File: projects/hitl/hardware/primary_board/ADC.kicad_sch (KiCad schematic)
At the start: 33 parts, among them J11 CONN_01X03, J12 CONN_01X03, J16 CONN_01X03, J17 CONN_01X03, J18 CONN_01X03, J19 CONN_01X03, U6 AD7091R-5BRUZ, U7 MCP6001, U8 74HCT4051D

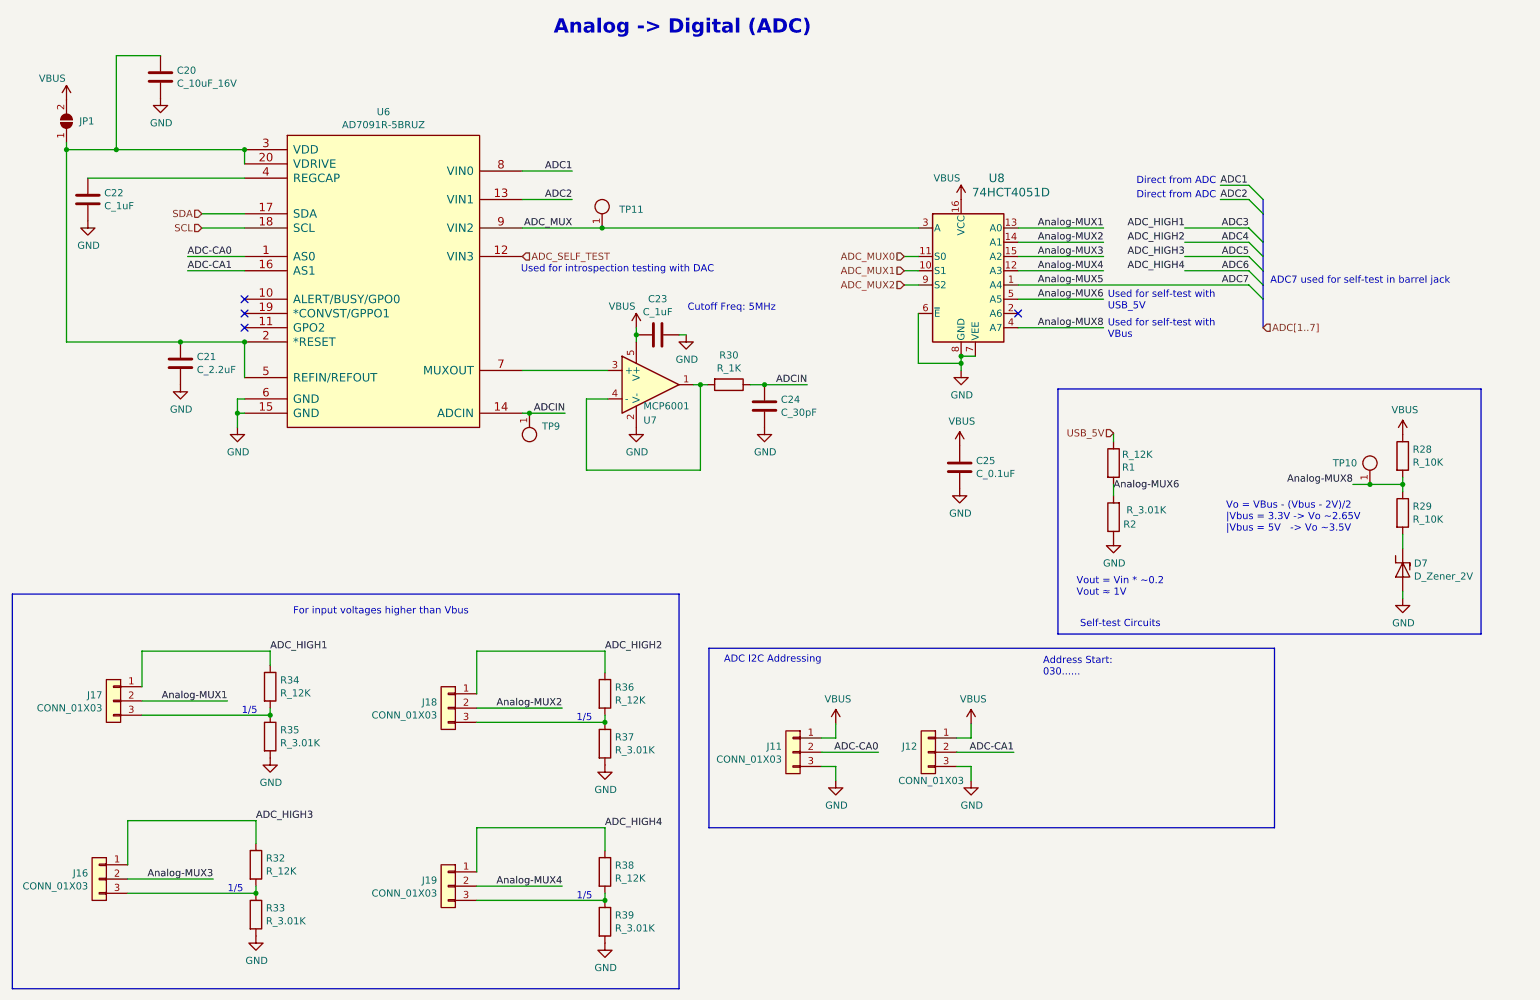
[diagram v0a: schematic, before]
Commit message: spec parts for hitl
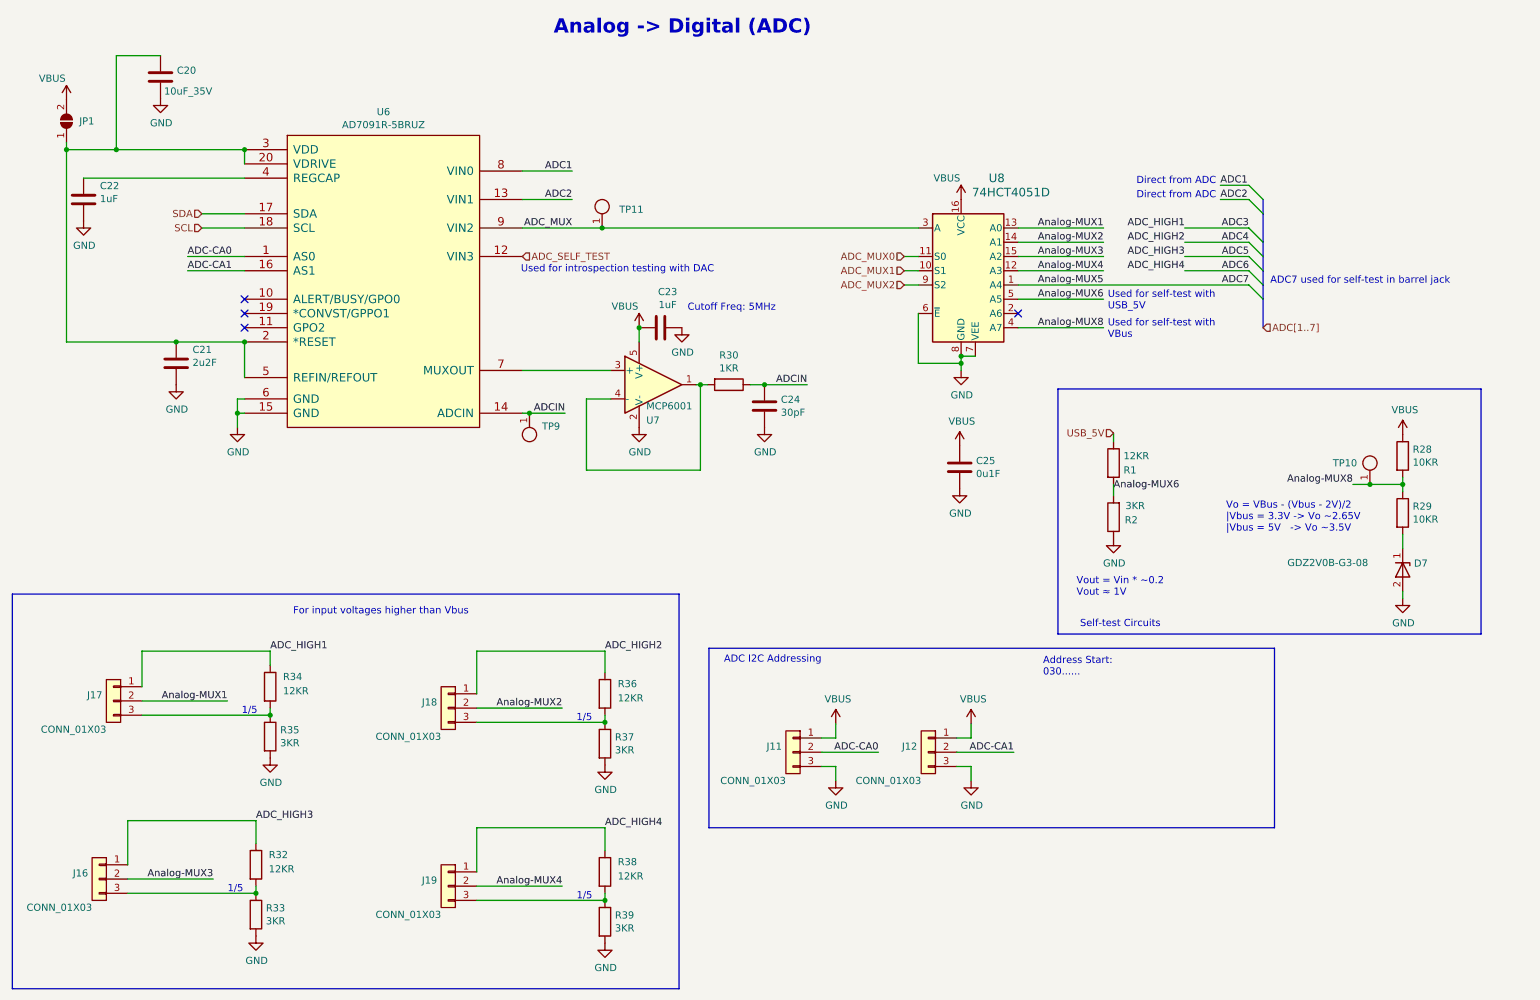
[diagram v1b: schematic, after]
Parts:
- C20: value C_10uF_16V -> 10uF_35V; footprint footprints:C_0805_OEM -> OEM:C_0603; symbol formula:C_10uF_16V -> OEM:10uF_35V; DKPN (none) -> 490-GRM188R6YA106MA73JDKR-ND; MFN DK -> Murata; MPN 1276-2399-1-ND -> GRM188R6YA106MA73J; NewDesigns (none) -> YES; Package (none) -> 0603; PurchasingLink https://www.digikey.com/product-detail/en/samsung-electro-m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 -> (none); Stocked (none) -> Digi-Reel; Style (none) -> SMD
- C21: value C_2.2uF -> 2u2F; footprint footprints:C_0805_OEM -> OEM:C_0603; symbol formula:C_2.2uF -> OEM:2u2F; DKPN (none) -> 490-GRM188R61E225KA12JDKR-ND; MFN (none) -> Murata; MPN (none) -> GRM188R61E225KA12J; NewDesigns (none) -> YES; Package (none) -> 0603; PurchasingLink https://www.digikey.com/product-detail/en/tdk-corporation/C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 -> (none); Stocked (none) -> Digi-Reel; Style (none) -> SMD
- C22, C23: value C_1uF -> 1uF; footprint footprints:C_0805_OEM -> OEM:C_0603; symbol formula:C_1uF -> OEM:1uF; DKPN (none) -> 1276-1184-2-ND; MFN (none) -> Samsung Electro-Mechanics; MPN (none) -> CL10B105KA8NNNC; NewDesigns (none) -> YES; Package (none) -> 0603; PurchasingLink https://www.digikey.com/product-detail/en/yageo/CC0805ZKY5V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 -> (none); Stocked (none) -> Reel; Style (none) -> SMD
- C24: value C_30pF -> 30pF; footprint footprints:C_0805_OEM -> OEM:C_0603; symbol formula:C_30pF -> OEM:30pF; DKPN (none) -> 738-CML0603C0G300JT50VDKR-ND; MFN DK -> Stackpole Electronics; MPN 1276-1130-1-ND -> CML0603C0G300JT50V; NewDesigns (none) -> YES; Package (none) -> 0603; PurchasingLink https://www.digikey.com/product-detail/en/samsung-electro-m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 -> (none); Stocked (none) -> Digi-Reel; Style (none) -> SMD
- C25: value C_0.1uF -> 0u1F; footprint footprints:C_0805_OEM -> OEM:C_0603; symbol formula:C_0.1uF -> OEM:0u1F; DKPN (none) -> 1276-1935-2-ND; MFN DK -> Samsung Electro-Mechanics; MPN 478-3352-1-ND -> CL10B104KB8NNWC; NewDesigns (none) -> YES; Package (none) -> 0603; PurchasingLink https://www.digikey.com/products/en?keywords=478-3352-1-ND -> (none); Stocked (none) -> Reel; Style (none) -> SMD
- D7: value D_Zener_2V -> GDZ2V0B-G3-08; symbol formula:D_Zener_2V -> OEM:GDZ2V0B-G3-08; DKPN (none) -> GDZ2V0B-G3-08GIDKR-ND; NewDesigns (none) -> YES; Package (none) -> SOD-323; PurchasingLink https://www.digikey.com/en/products/detail/vishay-general-s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 -> (none); Stocked (none) -> Digi-Reel; Style (none) -> SMD
- J11, J12, J16, J17, J18, J19: symbol formula:CONN_01X03 -> OEM:CONN_01X03; DKPN (none) -> 2057-PH1-03-UA-ND; MFN Mouser -> Adam Tech; MPN 855-M20-9990346 -> PH1-03-UA; NewDesigns (none) -> YES; Package (none) -> .1" pin header; PurchasingLink https://www.mouser.com/ProductDetail/Harwin/M20-9990346?qs=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 -> (none); Stocked (none) -> Bulk; Style (none) -> THT
- JP1: now left out of the parts list
- R1, R32, R34, R36, R38: value R_12K -> 12KR; footprint footprints:R_0805_OEM -> OEM:R_0603; symbol formula:R_12K -> OEM:12KR; DKPN (none) -> 1292-WR06X153JTLTR-ND; MFN TE -> Stackpole Electronics; MPN CRGP0805F12K -> RMCF0603FT12K0; NewDesigns (none) -> YES; Package (none) -> 0603; PurchasingLink https://www.digikey.com/en/products/detail/te-connectivity-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 -> (none); Stocked (none) -> Reel; Style (none) -> SMD
- R2, R33, R35, R37, R39: value R_3.01K -> 3KR; footprint footprints:R_0805_OEM -> OEM:R_0603; symbol formula:R_3.01K -> OEM:3KR; DKPN (none) -> 13-RC0603FR-103KLDKR-ND; MFN DK -> Yageo; MPN 311-3.01KCRCT-ND -> RC0603FR-103KL; NewDesigns (none) -> YES; Package (none) -> 0603; PurchasingLink https://www.digikey.com/products/en?keywords=311-3.01KCRCT-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 -> (none); Stocked (none) -> Digi-Reel; Style (none) -> SMD
- R28, R29: value R_10K -> 10KR; footprint footprints:R_0805_OEM -> OEM:R_0603; symbol formula:R_10K -> OEM:10KR; DKPN (none) -> RMCF0603FT10K0TR-ND; MFN DK -> Stackpole Electronics; MPN CRS0805-FX-1002ELFCT-ND -> RMCF0603FT10K0; NewDesigns (none) -> YES; Package (none) -> 0603; PurchasingLink https://www.digikey.com/products/en?keywords=CRS0805-FX-100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 -> (none); Stocked (none) -> Reel; Style (none) -> SMD
- R30: value R_1K -> 1KR; footprint footprints:R_0805_OEM -> OEM:R_0603; symbol formula:R_1K -> OEM:1KR; DKPN (none) -> RMCF0603FT1K00TR-ND; MFN DK -> Stackpole Electronics; MPN RNCP0805FTD1K00CT-ND -> RMCF0603FT1K00; NewDesigns (none) -> YES; Package (none) -> 0603; PurchasingLink https://www.digikey.com/products/en?keywords=RNCP0805FTD1K0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 -> (none); Stocked (none) -> Reel; Style (none) -> SMD
- TP10, TP11, TP9: value Test_Point_SMD -> TP_SMD; symbol formula:Test_Point_SMD -> OEM:TP_SMD; DKPN (none) -> 36-5019TR-ND; MFN (none) -> Keystone; MPN (none) -> 5019; NewDesigns (none) -> YES; Package (none) -> Custom; Stocked (none) -> Reel; Style (none) -> SMD
- U7: footprint footprints:SOT-23-5_OEM -> OEM:SOT-23-5; symbol formula:MCP6001 -> OEM:MCP6001; DKPN (none) -> MCP6001T-I/OTCT-ND; MFN DK -> Microchip; MPN MCP6001T-I/OTCT-ND -> MCP6001T-I/OT; NewDesigns (none) -> YES; Package (none) -> SOT23-5; PurchasingLink https://www.digikey.com/product-detail/en/microchip-technol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 -> (none); Stocked (none) -> Tape; Style (none) -> SMD
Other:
- moved on the sheet: C21, C22, C23, U7

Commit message: generate gerbs, fix leds and mcp6001s
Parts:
- U7: footprint OEM:SOT-23-5 -> Package_TO_SOT_SMD:SOT-353_SC-70-5; Package SOT23-5 -> SC-70-5
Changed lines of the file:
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@@
       (effects (font (size 1.27 1.27)) (justify left))
     )
-    (property "Footprint" "OEM:SOT-23-5" (id 2) (at 132.08 83.82 0)
+    (property "Footprint" "Package_TO_SOT_SMD:SOT-353_SC-70-5" (id 2) (at 132.08 83.82 0)
       (effects (font (size 1.27 1.27)) hide)
     )
@@
       (effects (font (size 1.27 1.27)) hide)
     )
-    (property "Package" "SOT23-5" (id 7) (at 134.62 86.36 0)
+    (property "Package" "SC-70-5" (id 7) (at 134.62 86.36 0)
       (effects (font (size 1.27 1.27)) hide)
     )
